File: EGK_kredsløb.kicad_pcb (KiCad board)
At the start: 2 copper layers, 100 x 70 mm, 68 parts, among them J1 USB4085-GF-A_REVB, J2 Conn_01x01_Pin, J3 Conn_01x01_Pin, J4 Conn_01x03, J5 Conn_01x01_Pin, J6 Conn_01x06_Pin, J7 10118194-0001LF, J8 Mini_Jack_5pins, U1 MCP6004, U2 MCP6004, U3 INA114AP, U4 MCP3208

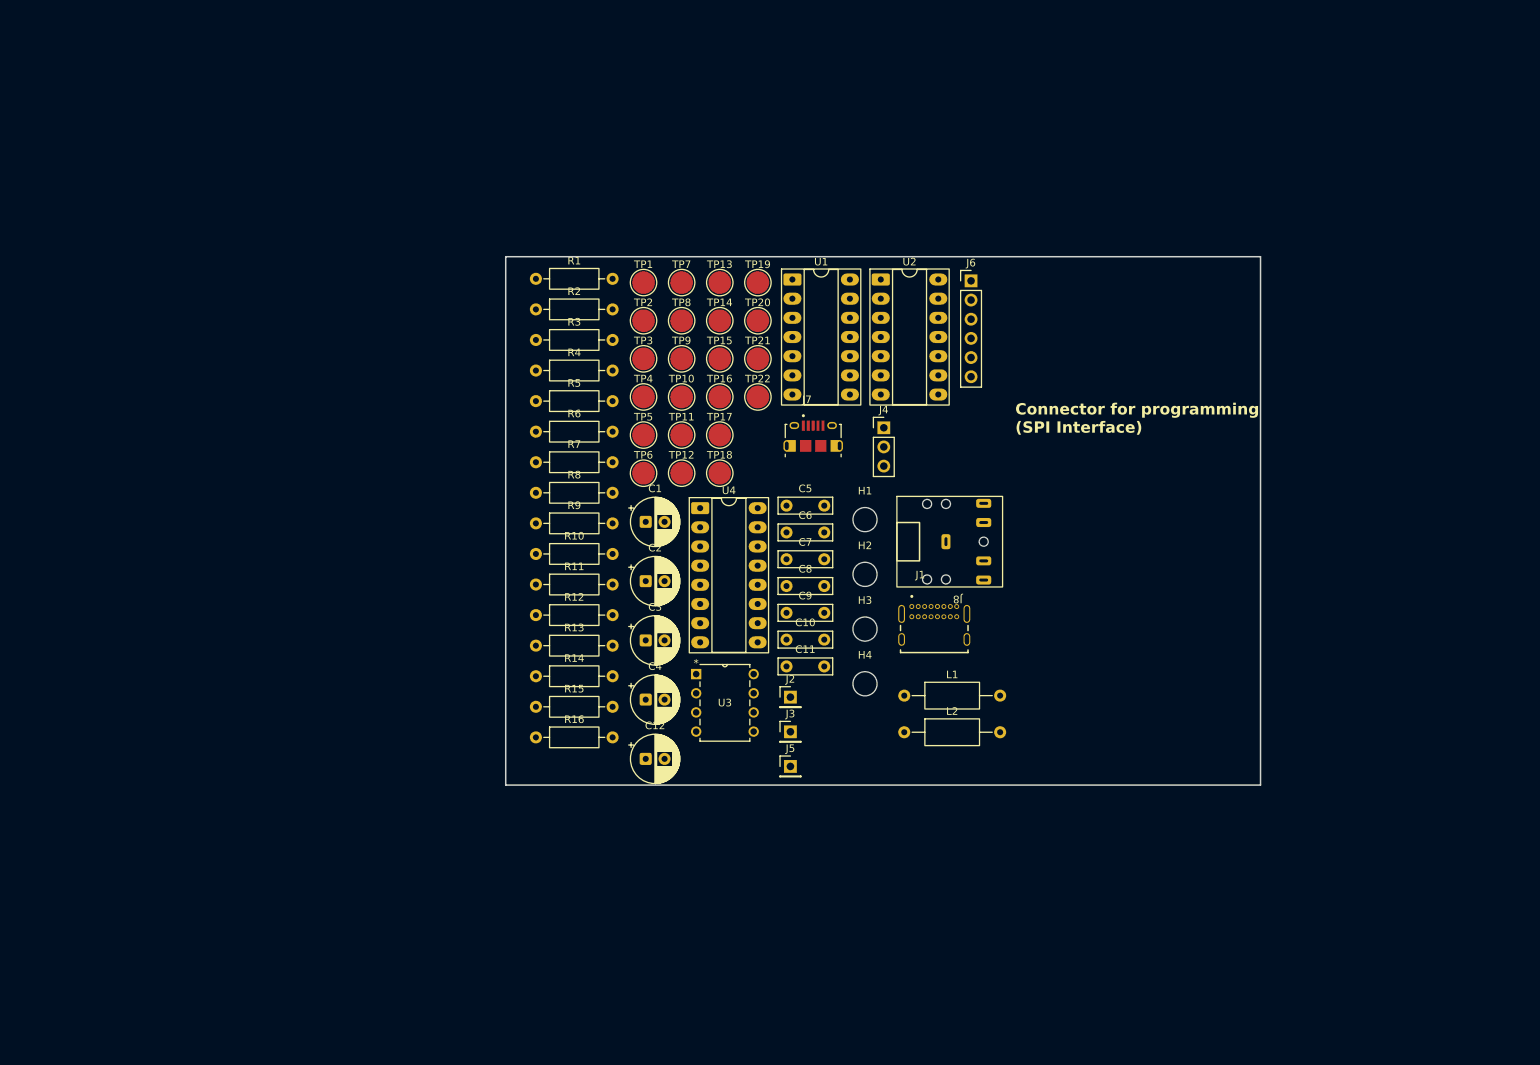
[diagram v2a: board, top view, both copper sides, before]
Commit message: Add layout floorplan ready for routing
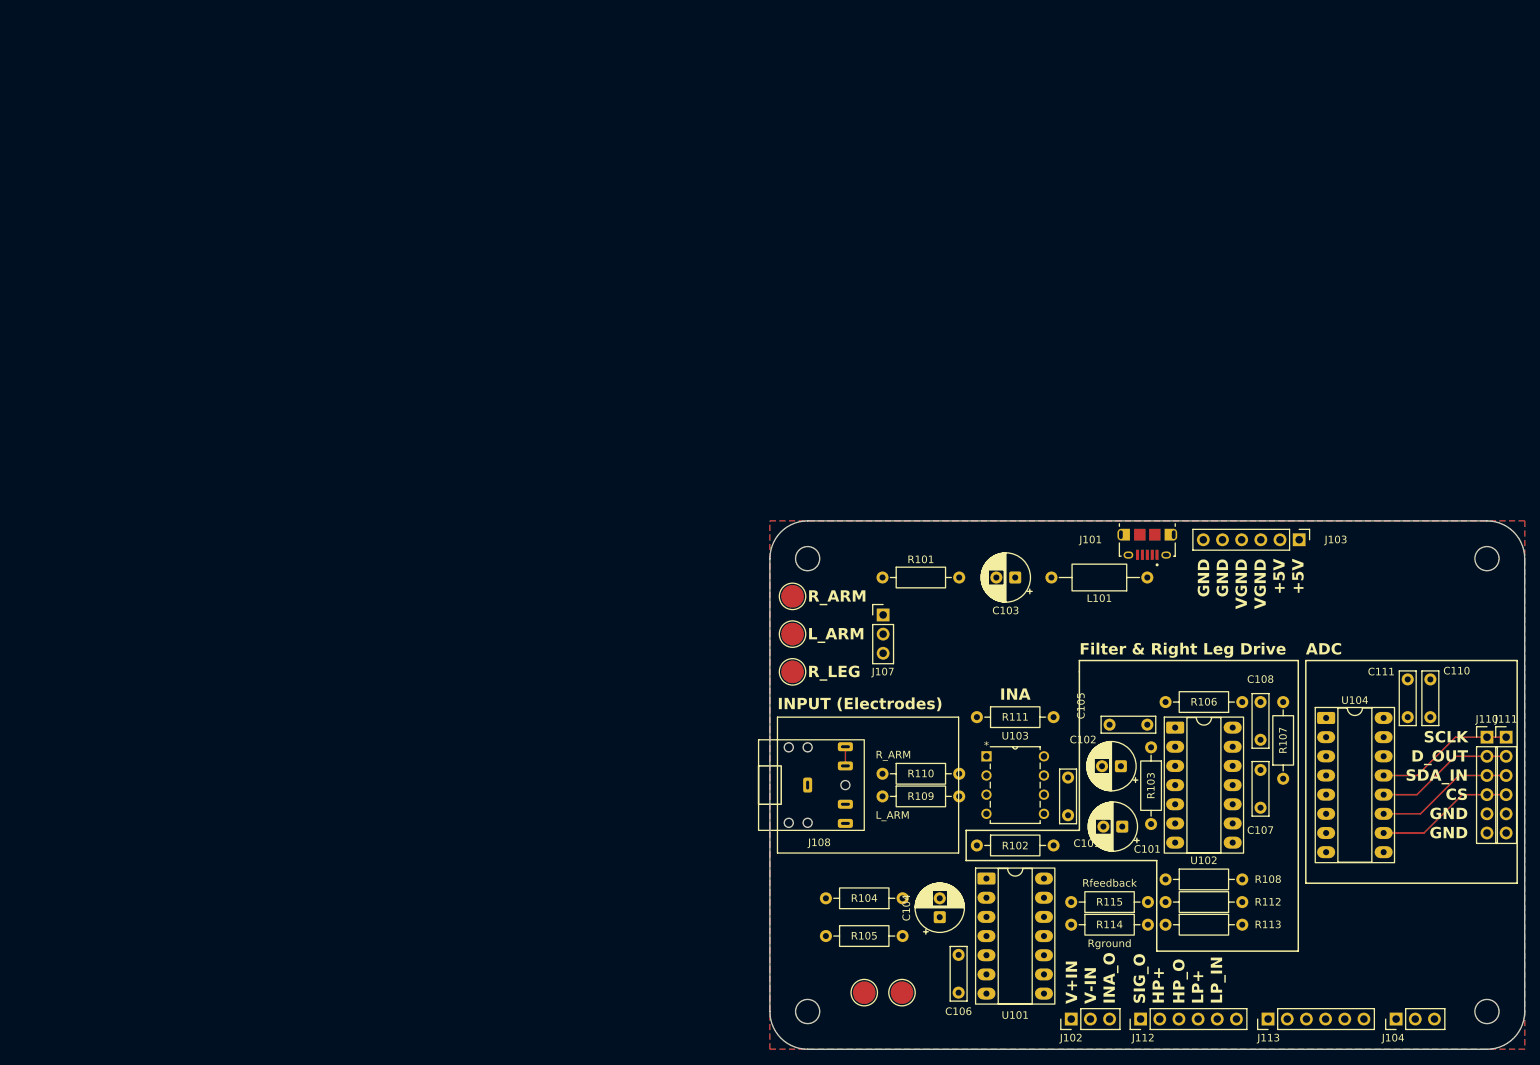
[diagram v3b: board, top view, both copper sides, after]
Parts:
- removed C1, C12, C2, C3: 10μ, Capacitor_THT:CP_Radial_D6.3mm_P2.50mm
- removed C10, C5, C6, C9: 100n, Capacitor_THT:C_Rect_L7.0mm_W2.0mm_P5.00mm
- removed C11: 10n, Capacitor_THT:C_Rect_L7.0mm_W2.0mm_P5.00mm
- removed C4: 1μ, Capacitor_THT:CP_Radial_D6.3mm_P2.50mm
- removed C7: 150n, Capacitor_THT:C_Rect_L7.0mm_W2.0mm_P5.00mm
- removed C8: 300n, Capacitor_THT:C_Rect_L7.0mm_W2.0mm_P5.00mm
- removed H1, H2, H3, H4: MountingHole, MountingHole:MountingHole_3.2mm_M3_ISO7380
- removed J1: USB4085-GF-A_REVB, connector:GCT_USB4085-GF-A_REVB
- removed J2, J3, J5: Conn_01x01_Pin, Connector_PinHeader_2.54mm:PinHeader_1x01_P2.54mm_Vertical
- removed J4: Conn_01x03, Connector_PinHeader_2.54mm:PinHeader_1x03_P2.54mm_Vertical
- removed J6: Conn_01x06_Pin, Connector_PinHeader_2.54mm:PinHeader_1x06_P2.54mm_Vertical
- removed J7: 10118194-0001LF, connector:AMPHENOL_10118194-0001LF
- removed J8: Mini_Jack_5pins, mini_jack_5pins.kicad_mod:mini_jack_5pins
- removed L1, L2: 1m, Inductor_THT:L_Axial_L7.0mm_D3.3mm_P12.70mm_Horizontal_Fastron_MICC
- removed R1, R16: 20, Resistor_THT:R_Axial_DIN0207_L6.3mm_D2.5mm_P10.16mm_Horizontal
- removed R10, R9: 100k, Resistor_THT:R_Axial_DIN0207_L6.3mm_D2.5mm_P10.16mm_Horizontal
- removed R11: 51, Resistor_THT:R_Axial_DIN0207_L6.3mm_D2.5mm_P10.16mm_Horizontal
- removed R12, R13: 390k, Resistor_THT:R_Axial_DIN0207_L6.3mm_D2.5mm_P10.16mm_Horizontal
- removed R14, R15, R8: 10k, Resistor_THT:R_Axial_DIN0207_L6.3mm_D2.5mm_P10.16mm_Horizontal
- removed R2: 470k, Resistor_THT:R_Axial_DIN0207_L6.3mm_D2.5mm_P10.16mm_Horizontal
- removed R3: 240k, Resistor_THT:R_Axial_DIN0207_L6.3mm_D2.5mm_P10.16mm_Horizontal
- removed R4, R5: 15k, Resistor_THT:R_Axial_DIN0207_L6.3mm_D2.5mm_P10.16mm_Horizontal
- removed R6, R7: 7.5k, Resistor_THT:R_Axial_DIN0207_L6.3mm_D2.5mm_P10.16mm_Horizontal
- removed TP1, TP10, TP11, TP12, TP13, TP14, TP15, TP16, TP17, TP18, TP19, TP2, TP20, TP21, TP22, TP3, TP4, TP5, TP6, TP7, TP8, TP9: TestPoint, TestPoint:TestPoint_Pad_D3.0mm
- removed U1, U2: MCP6004, Package_DIP:DIP-14_W7.62mm_Socket_LongPads
- removed U3: INA114AP, packages:PDIP8
- removed U4: MCP3208, Package_DIP:DIP-16_W7.62mm_Socket_LongPads
- added C101: 10μ, Capacitor_THT:CP_Radial_D6.3mm_P2.50mm, F.Cu at (146.7, 105.5)
- added C102: 10μ, Capacitor_THT:CP_Radial_D6.3mm_P2.50mm, F.Cu at (146.5, 97.5)
- added C103: 10μ, Capacitor_THT:CP_Radial_D6.3mm_P2.50mm, F.Cu at (132.5, 72.5)
- added C104: 1μ, Capacitor_THT:CP_Radial_D6.3mm_P2.50mm, F.Cu at (122.5, 117.5)
- added C105: 100n, Capacitor_THT:C_Rect_L7.0mm_W2.0mm_P5.00mm, F.Cu at (150.0, 92.0)
- added C106: 100n, Capacitor_THT:C_Rect_L7.0mm_W2.0mm_P5.00mm, F.Cu at (125.0, 122.5)
- added C107: 150n, Capacitor_THT:C_Rect_L7.0mm_W2.0mm_P5.00mm, F.Cu at (165.0, 103.0)
- added C108: 300n, Capacitor_THT:C_Rect_L7.0mm_W2.0mm_P5.00mm, F.Cu at (165.0, 89.0)
- added C109: 100n, Capacitor_THT:C_Rect_L7.0mm_W2.0mm_P5.00mm, F.Cu at (139.5, 99.0)
- added C110: 100n, Capacitor_THT:C_Rect_L7.0mm_W2.0mm_P5.00mm, F.Cu at (187.5, 91.0)
- added C111: 10n, Capacitor_THT:C_Rect_L7.0mm_W2.0mm_P5.00mm, F.Cu at (184.5, 91.0)
- added H101: MountingHole, MountingHole:MountingHole_3.2mm_M3_ISO7380, F.Cu at (105.0, 70.0)
- added H102: MountingHole, MountingHole:MountingHole_3.2mm_M3_ISO7380, F.Cu at (195.0, 70.0)
- added H103: MountingHole, MountingHole:MountingHole_3.2mm_M3_ISO7380, F.Cu at (195.0, 130.0)
- added H104: MountingHole, MountingHole:MountingHole_3.2mm_M3_ISO7380, F.Cu at (105.0, 130.0)
- added J101: 10118194-0001LF, connector:AMPHENOL_10118194-0001LF, F.Cu at (150.0, 66.8)
- added J102: Conn_01x03, Connector_PinHeader_2.54mm:PinHeader_1x03_P2.54mm_Vertical, F.Cu at (139.9, 131.0)
- added J103: Conn_01x06_Pin, Connector_PinHeader_2.54mm:PinHeader_1x06_P2.54mm_Vertical, F.Cu at (170.1, 67.5)
- added J104: Conn_01x03, Connector_PinHeader_2.54mm:PinHeader_1x03_P2.54mm_Vertical, F.Cu at (183.0, 131.0)
- added J107: Conn_01x03, Connector_PinHeader_2.54mm:PinHeader_1x03_P2.54mm_Vertical, F.Cu at (115.0, 77.5)
- added J108: Mini_Jack_5pins, connector:mini_jack_5pins, F.Cu at (110.0, 100.0)
- added J110: Conn_01x06_Pin, Connector_PinHeader_2.54mm:PinHeader_1x06_P2.54mm_Vertical, F.Cu at (195.0, 93.7)
- added J111: Conn_01x06_Pin, Connector_PinHeader_2.54mm:PinHeader_1x06_P2.54mm_Vertical, F.Cu at (197.5, 93.7)
- added J112: Conn_01x06_Pin, Connector_PinHeader_2.54mm:PinHeader_1x06_P2.54mm_Vertical, F.Cu at (149.1, 131.0)
- added J113: Conn_01x06_Pin, Connector_PinHeader_2.54mm:PinHeader_1x06_P2.54mm_Vertical, F.Cu at (166.0, 131.0)
- added L101: 1m, Inductor_THT:L_Axial_L7.0mm_D3.3mm_P12.70mm_Horizontal_Fastron_MICC, F.Cu at (150.0, 72.5)
- added R101: 20, Resistor_THT:R_Axial_DIN0207_L6.3mm_D2.5mm_P10.16mm_Horizontal, F.Cu at (114.9, 72.5)
- added R102: 470k, Resistor_THT:R_Axial_DIN0207_L6.3mm_D2.5mm_P10.16mm_Horizontal, F.Cu at (127.4, 108.0)
- added R103: 240k, Resistor_THT:R_Axial_DIN0207_L6.3mm_D2.5mm_P10.16mm_Horizontal, F.Cu at (150.5, 95.0)
- added R104: 15k, Resistor_THT:R_Axial_DIN0207_L6.3mm_D2.5mm_P10.16mm_Horizontal, F.Cu at (117.6, 115.0)
- added R105: 15k, Resistor_THT:R_Axial_DIN0207_L6.3mm_D2.5mm_P10.16mm_Horizontal, F.Cu at (107.4, 120.0)
- added R106: 7.5k, Resistor_THT:R_Axial_DIN0207_L6.3mm_D2.5mm_P10.16mm_Horizontal, F.Cu at (162.6, 89.0)
- added R107: 7.5k, Resistor_THT:R_Axial_DIN0207_L6.3mm_D2.5mm_P10.16mm_Horizontal, F.Cu at (168.0, 99.2)
- added R108: 10k, Resistor_THT:R_Axial_DIN0207_L6.3mm_D2.5mm_P10.16mm_Horizontal, F.Cu at (152.4, 112.5)
- added R109: 100k, Resistor_THT:R_Axial_DIN0207_L6.3mm_D2.5mm_P10.16mm_Horizontal, F.Cu at (114.9, 101.5)
- added R110: 100k, Resistor_THT:R_Axial_DIN0207_L6.3mm_D2.5mm_P10.16mm_Horizontal, F.Cu at (114.9, 98.5)
- added R111: 51, Resistor_THT:R_Axial_DIN0207_L6.3mm_D2.5mm_P10.16mm_Horizontal, F.Cu at (127.4, 91.0)
- added R112: 390k, Resistor_THT:R_Axial_DIN0207_L6.3mm_D2.5mm_P10.16mm_Horizontal, F.Cu at (162.6, 115.5)
- added R113: 390k, Resistor_THT:R_Axial_DIN0207_L6.3mm_D2.5mm_P10.16mm_Horizontal, F.Cu at (152.4, 118.5)
- added R114: 10k, Resistor_THT:R_Axial_DIN0207_L6.3mm_D2.5mm_P10.16mm_Horizontal, F.Cu at (139.9, 118.5)
- added R115: 10k, Resistor_THT:R_Axial_DIN0207_L6.3mm_D2.5mm_P10.16mm_Horizontal, F.Cu at (150.1, 115.5)
- added TP109: TestPoint, TestPoint:TestPoint_Pad_D3.0mm, F.Cu at (103.0, 85.0)
- added TP110: TestPoint, TestPoint:TestPoint_Pad_D3.0mm, F.Cu at (103.0, 80.0)
- added TP111: TestPoint, TestPoint:TestPoint_Pad_D3.0mm, F.Cu at (103.0, 75.0)
- added TP120: TestPoint, TestPoint:TestPoint_Pad_D3.0mm, F.Cu at (112.5, 127.5)
- added TP121: TestPoint, TestPoint:TestPoint_Pad_D3.0mm, F.Cu at (117.5, 127.5)
- added U101: MCP6004, Package_DIP:DIP-14_W7.62mm_Socket_LongPads, F.Cu at (128.7, 112.4)
- added U102: MCP6004, Package_DIP:DIP-14_W7.62mm_Socket_LongPads, F.Cu at (153.7, 92.4)
- added U103: INA114AP, packages:PDIP8, F.Cu at (136.3, 103.8)
- added U104: MCP3208, Package_DIP:DIP-16_W7.62mm_Socket_LongPads, F.Cu at (173.7, 91.1)
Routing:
- net /SERIAL_CLK: track 0.00 -> 18.4 mm
- net /CHIP_SELECT: track 0.00 -> 18.3 mm
- net /SERIAL_DATA_IN: track 0.00 -> 18.3 mm
- net /DIGITAL_OUT: track 0.00 -> 18.3 mm
- net /R_ARM: track 0.00 -> 2.54 mm
- added copper zone on F.Cu, net +5V
- added copper zone on B.Cu, net GND
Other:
- outline, holes or cut-outs redrawn
- board text added: "+5V"
- board text added: "ADC"
- board text added: "CS"
- board text added: "D_OUT"
- board text added: "Filter & Right Leg Drive"
- board text added: "GND"
- board text added: "HP+"
- board text added: "HP_O"
- board text added: "INA"
- board text added: "INA_O"
- board text added: "INPUT (Electrodes)"
- board text added: "LP+"
- board text added: "LP_IN"
- board text added: "L_ARM"
- board text added: "R_ARM"
- board text added: "R_LEG"
- board text added: "Rfeedback"
- board text added: "Rground"
- board text added: "SCLK"
- board text added: "SDA_IN"
- board text added: "SIG_O"
- board text added: "V+IN"
- board text added: "V-IN"
- board text added: "VGND"
- board text removed: "Connector for programming (SPI Interface)"
